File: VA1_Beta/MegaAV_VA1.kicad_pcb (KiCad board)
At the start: 4 copper layers, 50 x 50 mm, 177 parts, among them CN1 MD-90SM_MD2, P1 SMD_Conn_01x01, U1 4070, U2 74HCT123, U3 TS924, U4 THS7374, U5 ICS501, U6 TS922, U7 TS924, U8 AD723

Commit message: Silkscreen change
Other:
- board text added: "Dev Team: Villahed94 RGBeter"
- board text removed: "Dev Team: Villahed94 Ace9921 RGBeter"
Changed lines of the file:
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@@
 			(psa4output no)
 			(plot_black_and_white yes)
+			(plotinvisibletext no)
 			(sketchpadsonfab no)
 			(plotpadnumbers no)
@@
 	)
 	(gr_line
-		(start 202 136)
-		(end 202 143.45)
+		(start 201.15 136.075)
+		(end 201.15 143.525)
 		(stroke
 			(width 0.1)
@@
 		)
 	)
-	(gr_text "Dev Team:\nVillahed94\nAce9921\nRGBeter\n"
+	(gr_text "Dev Team:\nVillahed94\nRGBeter\n"
 		(at 200.3 143.5 270)
 		(layer "B.SilkS")

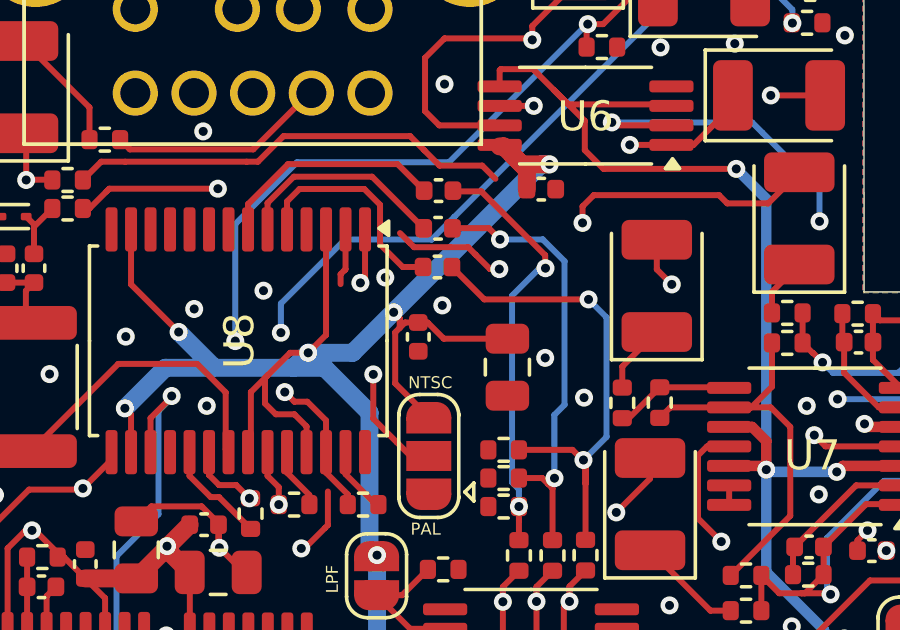
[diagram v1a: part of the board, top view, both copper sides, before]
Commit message: Silkscreen fix
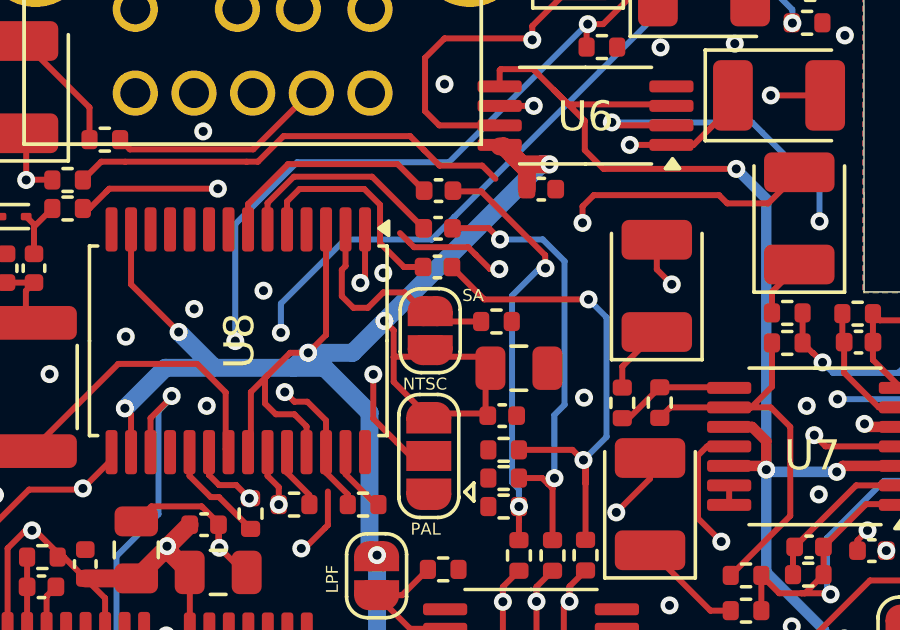
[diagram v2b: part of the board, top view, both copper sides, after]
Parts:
- added G***: LOGO, LOGO_Library:RIP-Felix Logo(Small), B.Cu at (193.5, 140.9)
- added R72: 47k, Resistor_SMD:R_0402_1005Metric, F.Cu at (187.1, 110.3)
- added SA1: ~, Jumper:SolderJumper-2_P1.3mm_Open_RoundedPad1.0x1.5mm, F.Cu at (184.8, 110.6)
- moved C39 3.84 mm to (187.2, 113.5), turned to 180 degrees
- moved C38 0.39 mm to (187.8, 111.9), turned to 180 degrees
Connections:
- U8 pad 2: GND -> Net-(SA1-B)
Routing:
- net Net-(SA1-B): track 0.00 -> 7.70 mm
- net +5V: track 270.3 -> 272.8 mm
- net GND: track 56.3 -> 54.4 mm, vias 76 -> 74
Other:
- board text added: "JUMPER SETTINGS: MD1 VA0-6.8: 1 C MD1 VA7, MD2 VA3: 2 C [-01, 2 F] MD2 VA0-1.8: 2 C D [-01, 2 F D] MD2 VA2-2.3: 1 B MD2 VA4: 2 A MD3: 2 A D REGION SELECT: Bridge PAL Or NTSC Jumper Bridge SA for PAL_M If you LIFTED RGB Legs: MD1PU HEADPHONE OUT: MD1 VA0-VA6.8: Y MD1 VA7, CDX, NOMAD, MEGA JET: Z NO HEADPHONE OUT: Y & SHORT HP P1 AND HP P2"
- board text added: "SA"
- board text removed: "JUMPER SETTINGS: MD1 VA0-6.8: 1 C MD1 VA7, MD2 VA3: 2 C [-01, 2 F] MD2 VA0-1.8: 2 C D [-01, 2 F D] MD2 VA2-2.3: 1 B MD2 VA4: 2 A MD3: 2 A D REGION SELECT: Bridge PAL Or NTSC Jumper If you LIFTED RGB Legs: MD1PU HEADPHONE OUT: MD1 VA0-VA6.8: Y MD1 VA7, CDX, NOMAD, MEGA JET: Z NO HEADPHONE OUT: Y & SHORT HP P1 AND HP P2"
